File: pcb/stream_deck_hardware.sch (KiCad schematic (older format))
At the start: 32 parts, among them J2 USB_C_Receptacle_USB2.0, J3 Conn_01x04_Male, J4 Conn_01x04_Male, U1 LF33_TO252, U2 STM32F401RCTx, U3 74LVC1G332, U4 AT24CS02-STUM, U5 AT24CS02-STUM, Y1 Crystal_Small

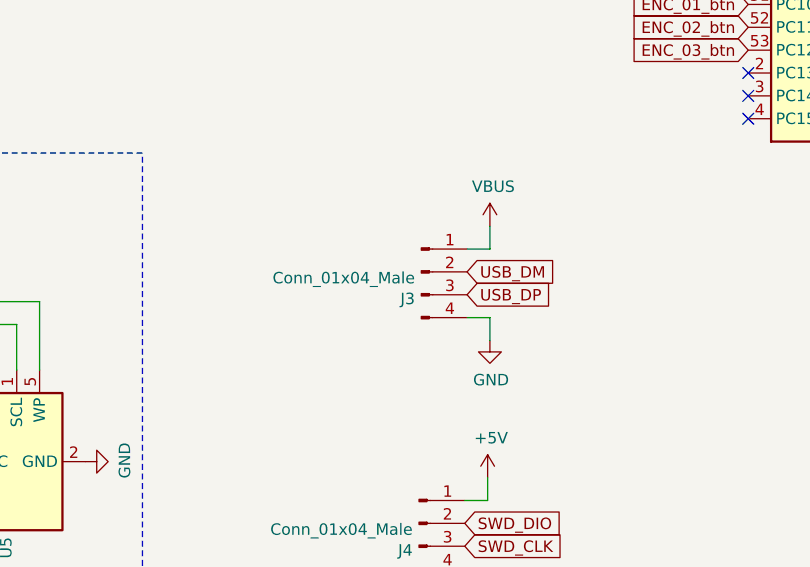
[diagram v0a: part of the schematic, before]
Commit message: Remove usb wire connector
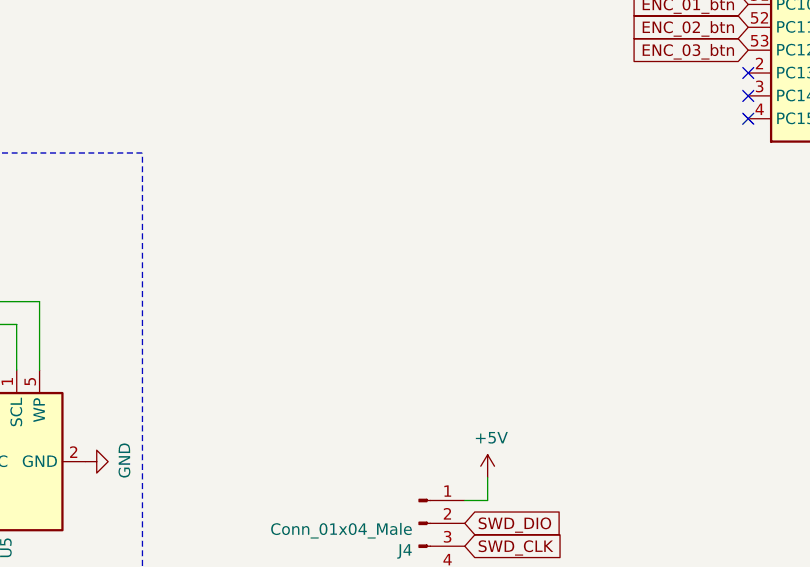
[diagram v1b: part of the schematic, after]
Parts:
- removed J3: Conn_01x04_Male, Connector_Wire:SolderWire-0.1sqmm_1x04_P3.6mm_D0.4mm_OD1mm_Relief, symbol Connector:Conn_01x04_Male
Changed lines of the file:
@@
 Text GLabel 7550 4850 2    50   Input ~ 0
 AMBILIGHT_LEDS
-Text GLabel 5020 6020 2    50   Input ~ 0
-USB_DM
-Text GLabel 5020 6120 2    50   Input ~ 0
-USB_DP
 Text GLabel 7550 3650 2    50   Input ~ 0
 SWD_CLK
@@
 	5110 7320 5110 7420
 $Comp
-L Connector:Conn_01x04_Male J3
-U 1 1 61ADEEF8
-P 4820 6020
-F 0 "J3" H 4792 5902 50  0000 R CNN
-F 1 "Conn_01x04_Male" H 4792 5993 50  0000 R CNN
-F 2 "Connector_Wire:SolderWire-0.1sqmm_1x04_P3.6mm_D0.4mm_OD1mm_Relief" H 4820 6020 50  0001 C CNN
-F 3 "~" H 4820 6020 50  0001 C CNN
-	1    4820 6020
-	1    0    0    -1
-$EndComp
-$Comp
 L power:+5V #PWR014
 U 1 1 61AE1ABA
@@
 Wire Wire Line
 	2730 3040 2730 2940
-$Comp
-L power:VBUS #PWR023
-U 1 1 61AF1C39
-P 5120 5820
-F 0 "#PWR023" H 5120 5670 50  0001 C CNN
-F 1 "VBUS" H 5135 5993 50  0000 C CNN
-F 2 "" H 5120 5820 50  0001 C CNN
-F 3 "" H 5120 5820 50  0001 C CNN
-	1    5120 5820
-	1    0    0    -1
-$EndComp
-Wire Wire Line
-	5020 5920 5120 5920
-Wire Wire Line
-	5120 5920 5120 5820
-$Comp
-L power:GND #PWR024
-U 1 1 61AF8851
-P 5120 6320
-F 0 "#PWR024" H 5120 6070 50  0001 C CNN
-F 1 "GND" H 5125 6147 50  0000 C CNN
-F 2 "" H 5120 6320 50  0001 C CNN
-F 3 "" H 5120 6320 50  0001 C CNN
-	1    5120 6320
-	1    0    0    -1
-$EndComp
-Wire Wire Line
-	5020 6220 5120 6220
-Wire Wire Line
-	5120 6220 5120 6320
 Wire Wire Line
 	2030 3790 2080 3790

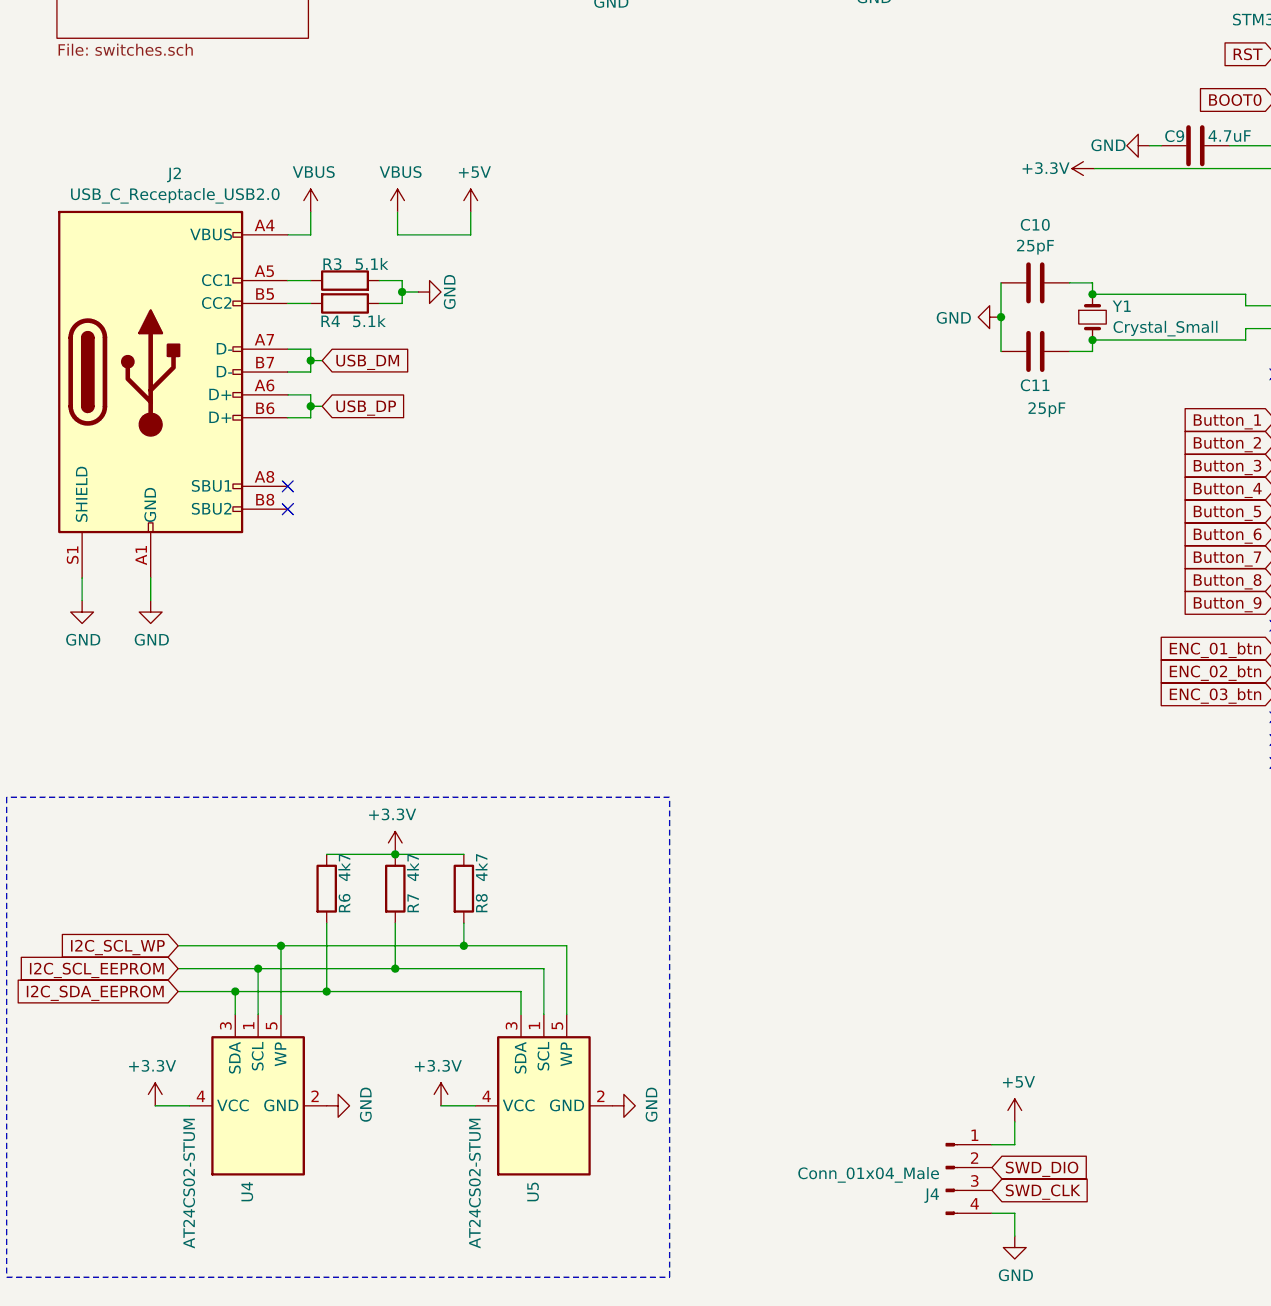
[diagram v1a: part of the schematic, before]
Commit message: Change connectors footprints
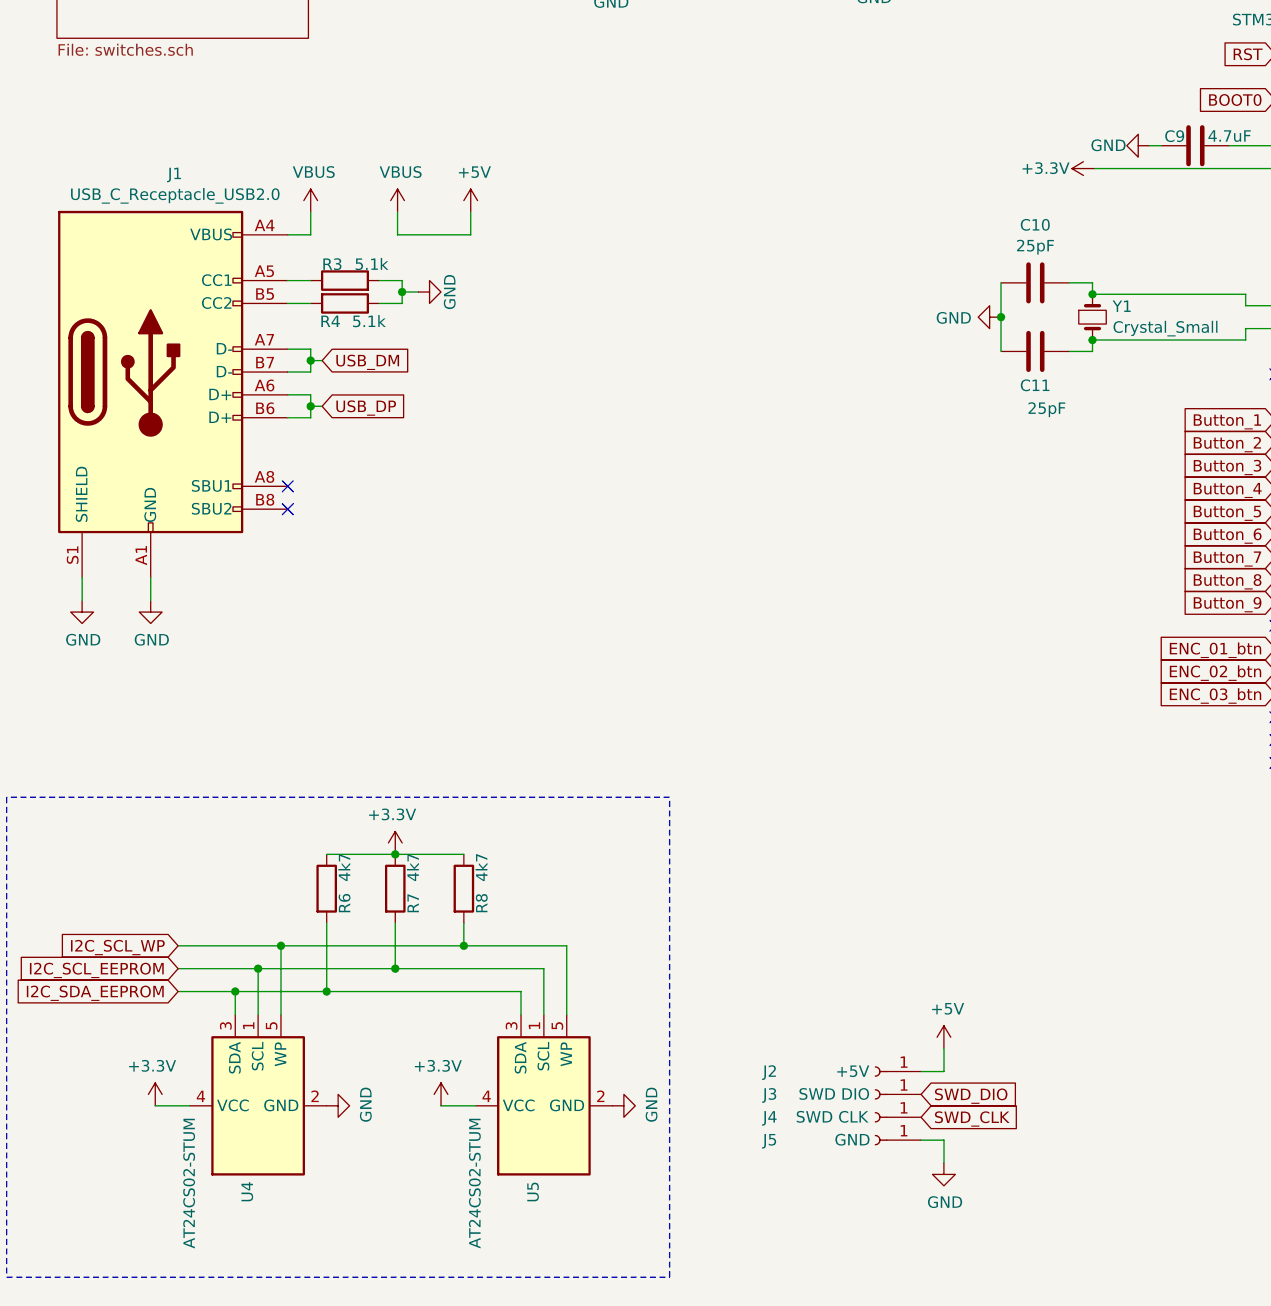
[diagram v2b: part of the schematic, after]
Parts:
- removed J4: Conn_01x04_Male, Connector_PinHeader_2.54mm:PinHeader_1x04_P2.54mm_Vertical, symbol Connector:Conn_01x04_Male
- added J2: +5V, TestPoint:TestPoint_Pad_D2.0mm, symbol Connector:Conn_01x01_Female
- added J3: SWD DIO, TestPoint:TestPoint_Pad_D2.0mm, symbol Connector:Conn_01x01_Female
- added J4: SWD CLK, TestPoint:TestPoint_Pad_D2.0mm, symbol Connector:Conn_01x01_Female
- added J5: GND, TestPoint:TestPoint_Pad_D2.0mm, symbol Connector:Conn_01x01_Female
- renumbered J2 to J1
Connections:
- net +5V: now also J2.1 (Pin_1)
- net GND: now also J5.1 (Pin_1)
- net SWD_CLK: now also J4.1 (Pin_1)
- net SWD_DIO: now also J3.1 (Pin_1)
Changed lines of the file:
@@
 	4640 1520 4740 1520
 $Comp
-L Connector:USB_C_Receptacle_USB2.0 J2
+L Connector:USB_C_Receptacle_USB2.0 J1
 U 1 1 6196C5CC
 P 1330 3640
-F 0 "J2" H 1437 4507 50  0000 C CNN
+F 0 "J1" H 1437 4507 50  0000 C CNN
 F 1 "USB_C_Receptacle_USB2.0" H 1437 4416 50  0000 C CNN
 F 2 "Connector_USB:USB_C_Receptacle_Palconn_UTC16-G" H 1480 3640 50  0001 C CNN
@@
 Text GLabel 7550 3550 2    50   Input ~ 0
 SWD_DIO
-Text GLabel 5010 7220 2    50   Input ~ 0
+Text GLabel 4700 6900 2    50   Input ~ 0
 SWD_CLK
-Text GLabel 5010 7120 2    50   Input ~ 0
+Text GLabel 4700 6800 2    50   Input ~ 0
 SWD_DIO
-$Comp
-L Connector:Conn_01x04_Male J4
-U 1 1 61ACAD72
-P 4810 7120
-F 0 "J4" H 4782 7002 50  0000 R CNN
-F 1 "Conn_01x04_Male" H 4782 7093 50  0000 R CNN
-F 2 "Connector_PinHeader_2.54mm:PinHeader_1x04_P2.54mm_Vertical" H 4810 7120 50  0001 C CNN
-F 3 "~" H 4810 7120 50  0001 C CNN
-	1    4810 7120
-	1    0    0    -1
-$EndComp
 $Comp
 L power:GND #PWR030
 U 1 1 61AD17C6
-P 5110 7420
-F 0 "#PWR030" H 5110 7170 50  0001 C CNN
-F 1 "GND" H 5115 7247 50  0000 C CNN
-F 2 "" H 5110 7420 50  0001 C CNN
-F 3 "" H 5110 7420 50  0001 C CNN
-	1    5110 7420
+P 4800 7100
+F 0 "#PWR030" H 4800 6850 50  0001 C CNN
+F 1 "GND" H 4805 6927 50  0000 C CNN
+F 2 "" H 4800 7100 50  0001 C CNN
+F 3 "" H 4800 7100 50  0001 C CNN
+	1    4800 7100
 	1    0    0    -1
 $EndComp
@@
 L power:+5V #PWR029
 U 1 1 61AD80BC
-P 5110 6920
-F 0 "#PWR029" H 5110 6770 50  0001 C CNN
-F 1 "+5V" H 5125 7093 50  0000 C CNN
-F 2 "" H 5110 6920 50  0001 C CNN
-F 3 "" H 5110 6920 50  0001 C CNN
-	1    5110 6920
-	1    0    0    -1
-$EndComp
-Wire Wire Line
-	5010 7020 5110 7020
-Wire Wire Line
-	5110 7020 5110 6920
-Wire Wire Line
-	5010 7320 5110 7320
-Wire Wire Line
-	5110 7320 5110 7420
+P 4800 6600
+F 0 "#PWR029" H 4800 6450 50  0001 C CNN
+F 1 "+5V" H 4815 6773 50  0000 C CNN
+F 2 "" H 4800 6600 50  0001 C CNN
+F 3 "" H 4800 6600 50  0001 C CNN
+	1    4800 6600
+	1    0    0    -1
+$EndComp
+Wire Wire Line
+	4700 6700 4800 6700
+Wire Wire Line
+	4800 6700 4800 6600
+Wire Wire Line
+	4700 7000 4800 7000
+Wire Wire Line
+	4800 7000 4800 7100
 $Comp
 L power:+5V #PWR014
@@
 Wire Wire Line
 	2030 3790 2030 3840
+$Comp
+L Connector:Conn_01x01_Female J2
+U 1 1 61EB39A0
+P 4500 6700
+F 0 "J2" H 4960 6700 50  0000 C CNN
+F 1 "+5V" H 4600 6700 50  0000 C CNN
+F 2 "TestPoint:TestPoint_Pad_D2.0mm" H 4500 6700 50  0001 C CNN
+F 3 "~" H 4500 6700 50  0001 C CNN
+	1    4500 6700
+	-1   0    0    1
+$EndComp
+$Comp
+L Connector:Conn_01x01_Female J3
+U 1 1 61EB4DFC
+P 4500 6800
+F 0 "J3" H 4960 6800 50  0000 C CNN
+F 1 "SWD DIO" H 4680 6800 50  0000 C CNN
+F 2 "TestPoint:TestPoint_Pad_D2.0mm" H 4500 6800 50  0001 C CNN
+F 3 "~" H 4500 6800 50  0001 C CNN
+	1    4500 6800
+	-1   0    0    1
+$EndComp
+$Comp
+L Connector:Conn_01x01_Female J4
+U 1 1 61EB916A
+P 4500 6900
+F 0 "J4" H 4960 6900 50  0000 C CNN
+F 1 "SWD CLK" H 4690 6900 50  0000 C CNN
+F 2 "TestPoint:TestPoint_Pad_D2.0mm" H 4500 6900 50  0001 C CNN
+F 3 "~" H 4500 6900 50  0001 C CNN
+	1    4500 6900
+	-1   0    0    1
+$EndComp
+$Comp
+L Connector:Conn_01x01_Female J5
+U 1 1 61EBD406
+P 4500 7000
+F 0 "J5" H 4960 7000 50  0000 C CNN
+F 1 "GND" H 4600 7000 50  0000 C CNN
+F 2 "TestPoint:TestPoint_Pad_D2.0mm" H 4500 7000 50  0001 C CNN
+F 3 "~" H 4500 7000 50  0001 C CNN
+	1    4500 7000
+	-1   0    0    1
+$EndComp
 $EndSCHEMATC

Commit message: Pads placement
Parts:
- JP4, JP5: footprint Jumper:SolderJumper-3_P1.3mm_Bridged2Bar12_RoundedPad1.0x1.5mm_NumberLabels -> Jumper:SolderJumper-3_P1.3mm_Open_RoundedPad1.0x1.5mm
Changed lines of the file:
@@
 F 0 "JP4" V 3304 1608 50  0000 L CNN
 F 1 "SolderJumper_3_Open" V 3395 1608 50  0000 L CNN
-F 2 "Jumper:SolderJumper-3_P1.3mm_Bridged2Bar12_RoundedPad1.0x1.5mm_NumberLabels" H 3350 1540 50  0001 C CNN
+F 2 "Jumper:SolderJumper-3_P1.3mm_Open_RoundedPad1.0x1.5mm" H 3350 1540 50  0001 C CNN
 F 3 "~" H 3350 1540 50  0001 C CNN
 	1    3350 1540
@@
 F 0 "JP5" V 4444 1588 50  0000 L CNN
 F 1 "SolderJumper_3_Open" V 4535 1588 50  0000 L CNN
-F 2 "Jumper:SolderJumper-3_P1.3mm_Bridged2Bar12_RoundedPad1.0x1.5mm_NumberLabels" H 4490 1520 50  0001 C CNN
+F 2 "Jumper:SolderJumper-3_P1.3mm_Open_RoundedPad1.0x1.5mm" H 4490 1520 50  0001 C CNN
 F 3 "~" H 4490 1520 50  0001 C CNN
 	1    4490 1520

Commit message: Bugfix
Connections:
- net USB_DM renamed USB_D-
- net USB_DP renamed USB_D+
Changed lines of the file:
@@
 	2030 3840 1930 3840
 Text GLabel 2080 3590 2    50   Input ~ 0
-USB_DM
+USB_D-
 Text GLabel 2080 3790 2    50   Input ~ 0
-USB_DP
+USB_D+
 Wire Wire Line
 	1930 3040 2030 3040
@@
 $EndComp
 Text GLabel 7550 3450 2    50   Input ~ 0
-USB_DM
-Text GLabel 7550 3350 2    50   Input ~ 0
-USB_DP
+USB_D-
 Wire Wire Line
 	6120 3300 6120 3350
@@
 	-1   0    0    1
 $EndComp
+Text GLabel 7550 3350 2    50   Input ~ 0
+USB_D+
 $EndSCHEMATC

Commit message: update
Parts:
- removed J2: +5V, TestPoint:TestPoint_Pad_D2.0mm, symbol Connector:Conn_01x01_Female
- removed J3: SWD DIO, TestPoint:TestPoint_Pad_D2.0mm, symbol Connector:Conn_01x01_Female
- removed J4: SWD CLK, TestPoint:TestPoint_Pad_D2.0mm, symbol Connector:Conn_01x01_Female
- removed J5: GND, TestPoint:TestPoint_Pad_D2.0mm, symbol Connector:Conn_01x01_Female
- added D?: LED, symbol Device:LED
- added D?: 3.3V_LED, symbol Device:LED
- added D?: 5V_LED, symbol Device:LED
- added J?: SWD, symbol Connector:Conn_01x04_Male
- added R? (x3): R, symbol Device:R
- added SW?: RESET, symbol Switch:SW_Push
- added TP?: D-, symbol Connector:TestPoint
- added TP?: D+, symbol Connector:TestPoint
- added TP? (x2): SCL, symbol Connector:TestPoint
- added TP?: SDA, symbol Connector:TestPoint
- added TP?: 3.3V, symbol Connector:TestPoint
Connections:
- net +3V3: now also R?.1, R?.1, TP?.1
- net +5V: now also J?.1 (Pin_1), R?.1
- net GND: now also D?.1 (K), D?.1 (K), J?.4 (Pin_4), SW?.1, TP?.1
- net I2C_SCL_EEPROM: now also TP?.1
- net I2C_SDA_EEPROM: now also TP?.1
- net RST: now also SW?.2
- net SWD_CLK: now also J?.3 (Pin_3)
- net SWD_DIO: now also J?.2 (Pin_2)
- net USB_D+: now also TP?.1
- net USB_D-: now also TP?.1
- net at U2.17 (PA3): now also D?.1 (K)
- new net: D?.2 (A), R?.2 (x3)
- no-connect marks 22 -> 21
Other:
- moved on the sheet: C12, R5, U3
